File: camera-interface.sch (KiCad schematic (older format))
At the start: 44 parts, among them J8 WE_68715014522, U19 NTS0102GT, U20 NTS0102GT, U22 AP2114H-3_3TRG1

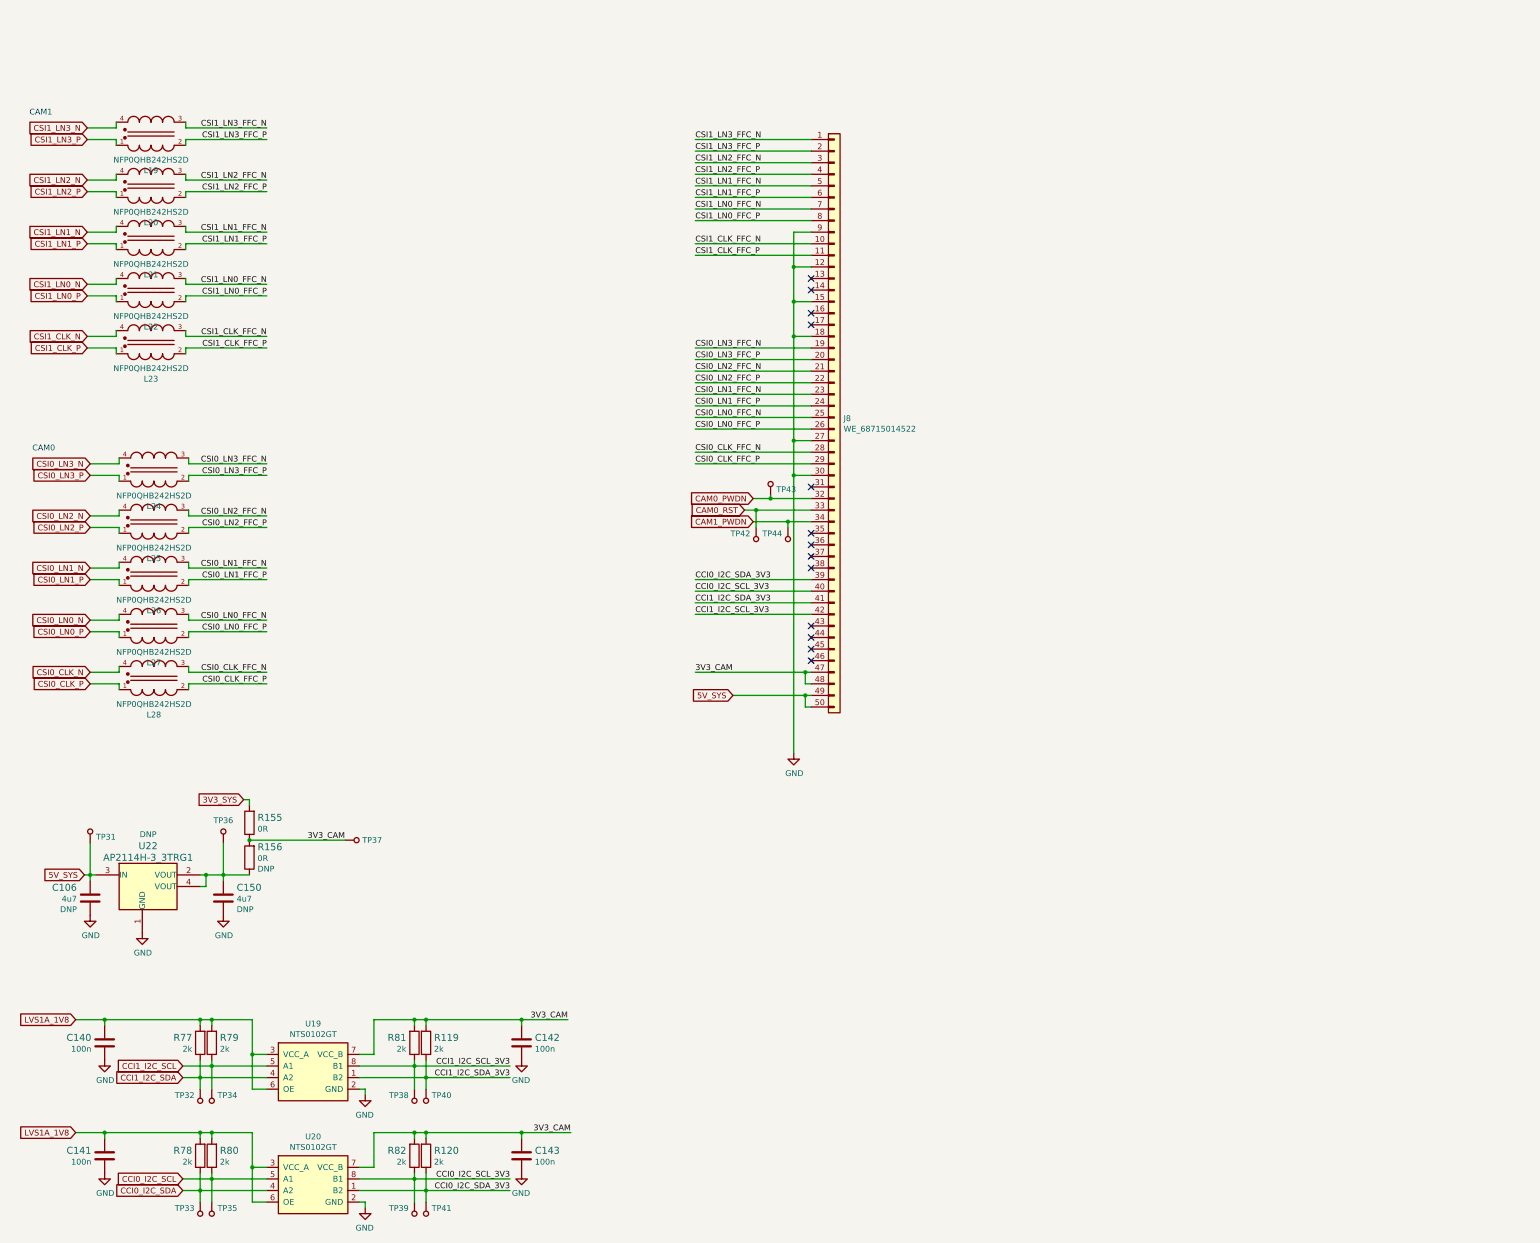
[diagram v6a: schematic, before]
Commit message: Reorganize schematics, add descriptions in top left corner
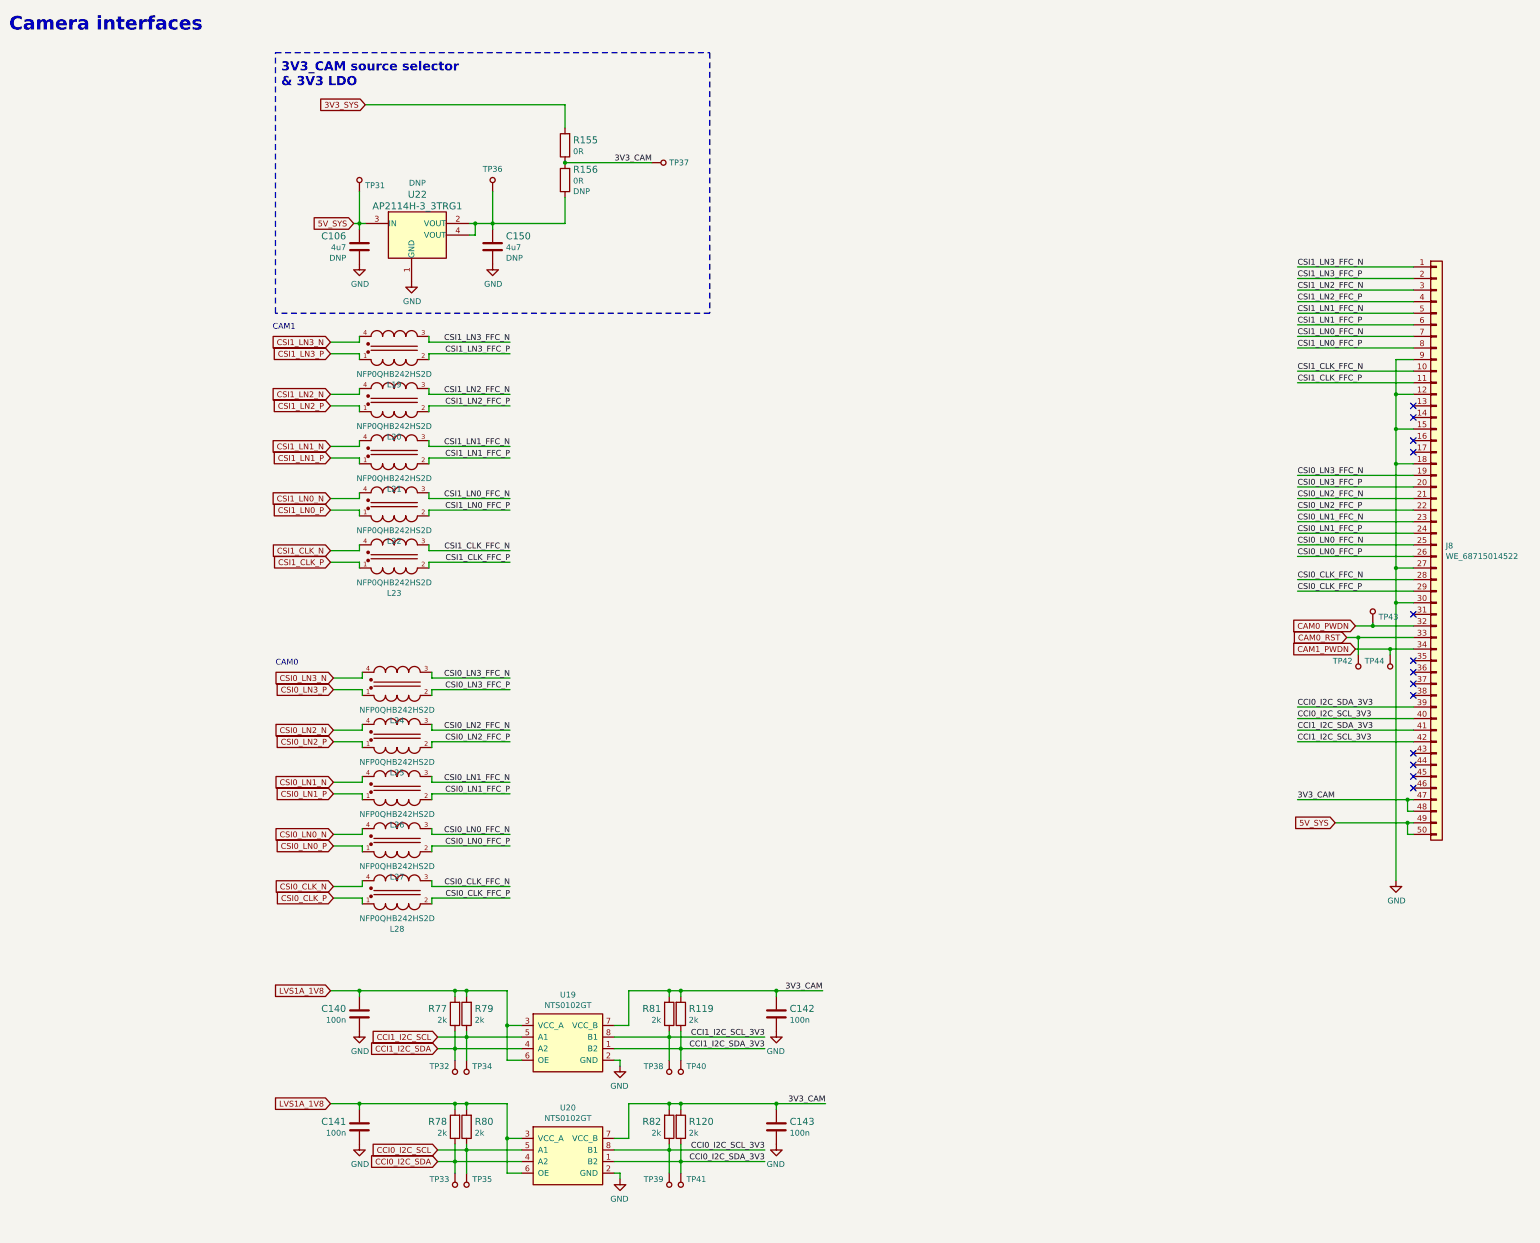
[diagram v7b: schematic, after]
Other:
- note added: "3V3_CAM source selector\n& 3V3 LDO"
- note added: "Camera interfaces"
- moved on the sheet: C106, C140, C141, C142, C143, C150, J8, L19, L20, L21, L22, L23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

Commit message: Clear annotation and annotate
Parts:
- renumbered C106 to C105, C140 to C106, C141 to C107, C150 to C108, C142 to C109, C143 to C110, J8 to J7, L19 to L16, L20 to L17, L21 to L18, L22 to L19, L23 to L20, L24 to L21, L25 to L22, L26 to L23, L27 to L24, L28 to L25, R77 to R80, R78 to R81, R79 to R82, R80 to R83, R155 to R84, R156 to R85, R81 to R86, R82 to R87, R119 to R88, R120 to R89, TP31 to TP28, TP32 to TP29, TP33 to TP30, TP34 to TP31, TP35 to TP32, TP36 to TP33, TP37 to TP34, TP38 to TP35, TP39 to TP36, TP40 to TP37, TP41 to TP38, TP42 to TP39, TP43 to TP40, TP44 to TP41, U22 to U12, U19 to U13, U20 to U14
